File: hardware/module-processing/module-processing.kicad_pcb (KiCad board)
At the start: 2 copper layers, 64 x 93.5 mm, 64 parts, among them IC1 PIC24FJ256GA702-I_SO, J1 Conn_02x10_Odd_Even, J2 Raspberry_Pi_2_3, J3 ICSP, Q1 Q_NPN_EBC, Q2 Q_NPN_EBC, Q3 Q_NPN_EBC, Q4 Q_NPN_EBC, U1 74HC595, Y1 MCSJK-7U-32.00-12-30-60-B-30

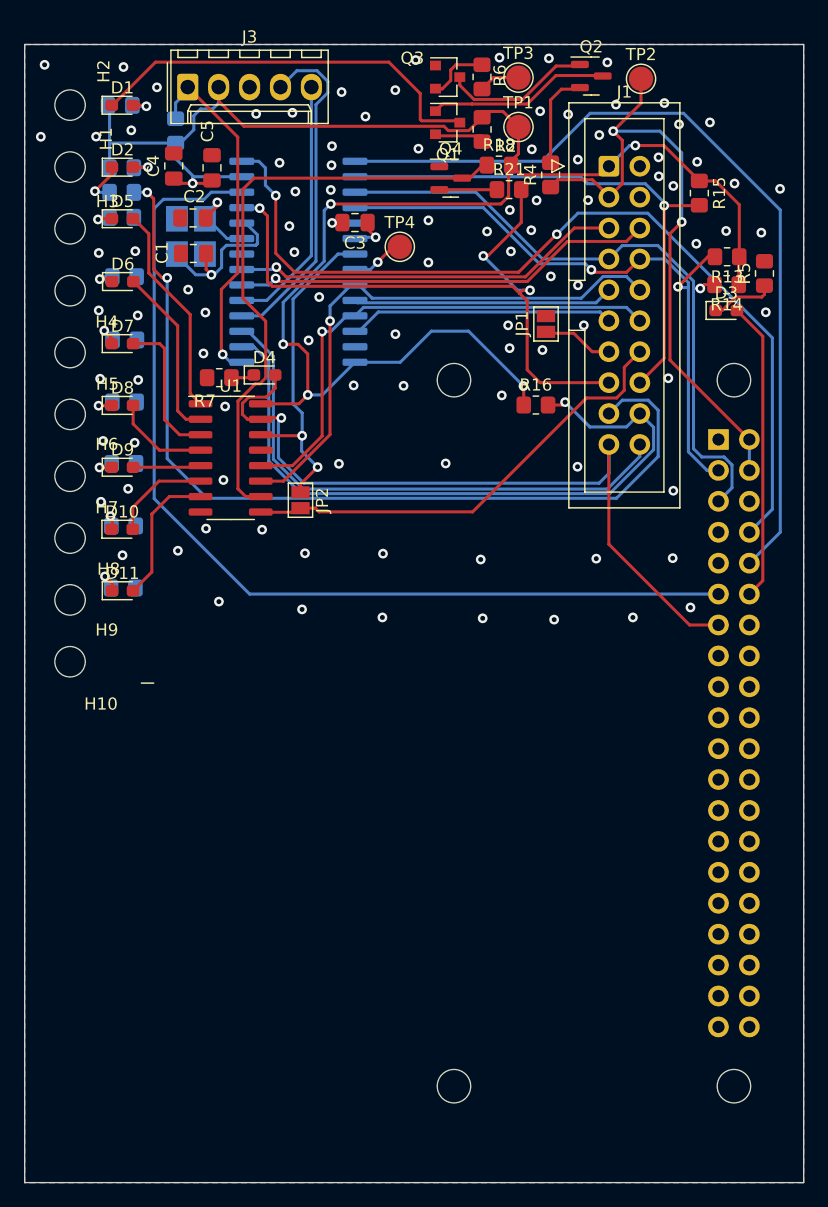
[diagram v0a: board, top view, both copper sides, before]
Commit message: fix: move pi to sensible position; chore: tidy and check
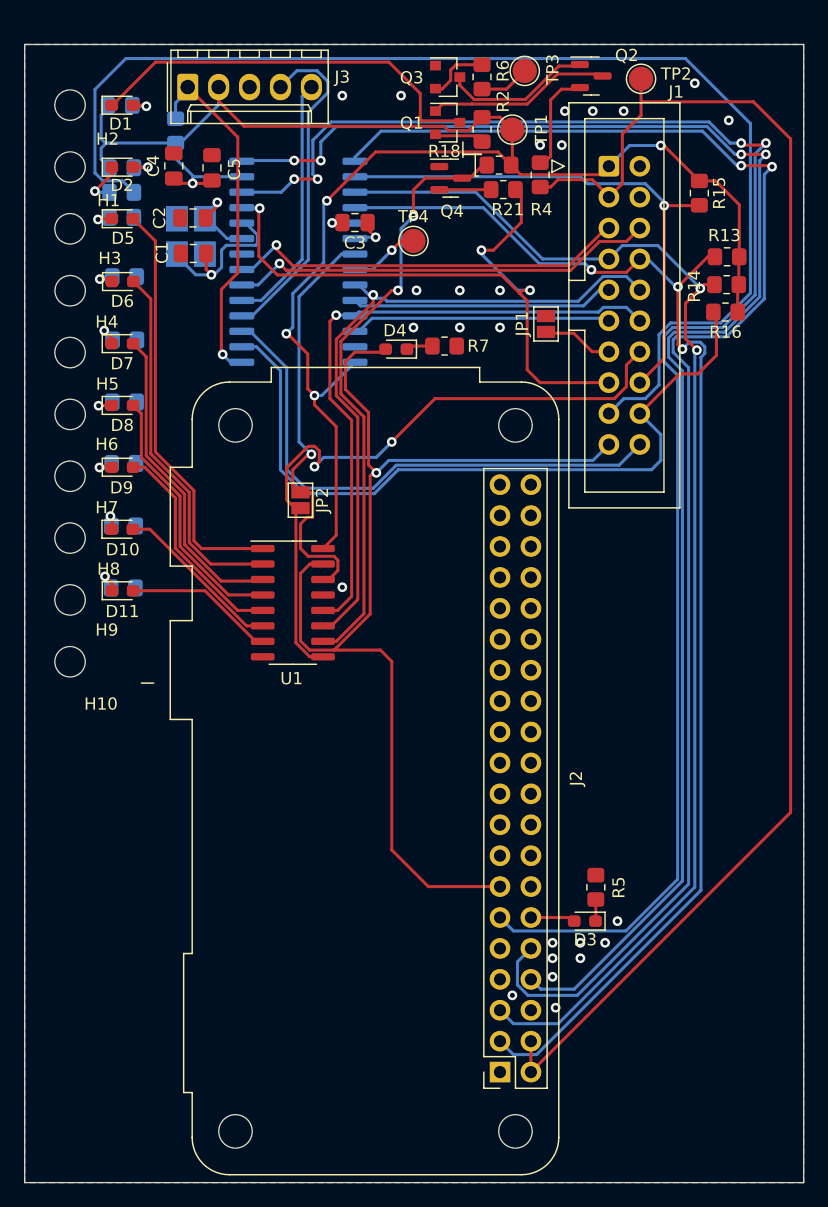
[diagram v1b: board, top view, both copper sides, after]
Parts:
- J2: moved to F.Cu
- moved J2 55.0 mm to (162.1, 108.9)
- moved R5 52.3 mm to (169.9, 93.7)
- moved D3 51.5 mm to (169.0, 96.5), turned to 180 degrees
- moved R7 18.7 mm to (157.5, 49.3), turned to 0 degrees
- moved R16 17.3 mm to (180.6, 46.5), turned to 180 degrees
- moved U1 12.9 mm to (145.0, 70.4)
- moved D4 11.0 mm to (153.5, 49.5), turned to 180 degrees
- moved TP4 1.22 mm to (154.9, 40.6)
- moved R4 0.86 mm to (165.4, 35.2)
- moved TP3 0.75 mm to (164.1, 26.7)
- moved TP1 0.55 mm to (163.1, 31.5)
- moved R21 0.48 mm to (162.3, 36.4)
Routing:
- net +5V: track 52.6 -> 118.8 mm, vias 2 -> 0
- net /Backplane/SDA: track 52.8 -> 108.4 mm, vias 2 -> 3
- net /Pi/PI_TX: track 74.0 -> 128.1 mm, vias 2 -> 4
- net /Pi/PI_RX: track 69.9 -> 123.6 mm, vias 0 -> 2
- net /Pi/PI_IO: track 81.2 -> 132.5 mm, vias 0 -> 4
- net /Backplane/SCL: track 54.6 -> 105.1 mm, vias 1 -> 2
- net /Backplane/HBEAT: track 62.5 -> 91.2 mm
- net /Backplane/ID_RET: track 75.6 -> 99.9 mm, vias 2 -> 0
- net /Pi/PI_HBEAT: track 24.6 -> 3.26 mm
- net Net-(D5-Pad2): track 17.5 -> 34.4 mm
- net /Backplane/OUT_DO: track 37.5 -> 53.7 mm, vias 0 -> 2
- net Net-(D6-Pad2): track 14.3 -> 30.1 mm
- net Net-(D7-Pad2): track 12.1 -> 25.8 mm
- net Net-(D8-Pad2): track 7.95 -> 21.6 mm
- net Net-(D9-Pad2): track 5.32 -> 17.9 mm
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
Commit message: feat: add labels to io pcb; feat: add labels to cpu pcb
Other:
- board text added: "PLC Processor Module V1.0 02/22 AGSB (C) Trace Technical Services"
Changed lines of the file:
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@@
     (fp_line (start -1 -0.625) (end 1 -0.625) (layer "F.Fab") (width 0.1))
     (fp_line (start 1 0.625) (end -1 0.625) (layer "F.Fab") (width 0.1))
-    (pad "1" smd roundrect (at -1 0 90) (size 1.2 1.4) (layers "F.Cu" "F.Paste" "F.Mask") (roundrect_rratio 0.208333)
+    (pad "1" smd roundrect (at -1 0 90) (size 1.2 1.4) (layers "F.Cu" "F.Paste" "F.Mask") (roundrect_rratio 0.2083333333)
       (net 7 "Net-(D3-Pad1)") (pintype "passive"))
-    (pad "2" smd roundrect (at 1 0 90) (size 1.2 1.4) (layers "F.Cu" "F.Paste" "F.Mask") (roundrect_rratio 0.208333)
+    (pad "2" smd roundrect (at 1 0 90) (size 1.2 1.4) (layers "F.Cu" "F.Paste" "F.Mask") (roundrect_rratio 0.2083333333)
       (net 1 "0") (pintype "passive"))
     (model "${KICAD6_3DMODEL_DIR}/Resistor_SMD.3dshapes/R_0805_2012Metric.wrl"
@@
     (fp_line (start 1 -0.625) (end 1 0.625) (layer "F.Fab") (width 0.1))
     (fp_line (start -1 -0.625) (end 1 -0.625) (layer "F.Fab") (width 0.1))
-    (pad "1" smd roundrect (at -1 0) (size 1.2 1.4) (layers "F.Cu" "F.Paste" "F.Mask") (roundrect_rratio 0.208333)
+    (pad "1" smd roundrect (at -1 0) (size 1.2 1.4) (layers "F.Cu" "F.Paste" "F.Mask") (roundrect_rratio 0.2083333333)
       (net 80 "Net-(Q4-Pad2)") (pintype "passive"))
-    (pad "2" smd roundrect (at 1 0) (size 1.2 1.4) (layers "F.Cu" "F.Paste" "F.Mask") (roundrect_rratio 0.208333)
+    (pad "2" smd roundrect (at 1 0) (size 1.2 1.4) (layers "F.Cu" "F.Paste" "F.Mask") (roundrect_rratio 0.2083333333)
       (net 22 "/Backplane/RESET") (pintype "passive"))
     (model "${KICAD6_3DMODEL_DIR}/Resistor_SMD.3dshapes/R_0805_2012Metric.wrl"
@@
     (fp_line (start -1 -0.625) (end 1 -0.625) (layer "F.Fab") (width 0.1))
     (fp_line (start 1 -0.625) (end 1 0.625) (layer "F.Fab") (width 0.1))
-    (pad "1" smd roundrect (at -1 0 180) (size 1.2 1.4) (layers "F.Cu" "F.Paste" "F.Mask") (roundrect_rratio 0.208333)
+    (pad "1" smd roundrect (at -1 0 180) (size 1.2 1.4) (layers "F.Cu" "F.Paste" "F.Mask") (roundrect_rratio 0.2083333333)
       (net 2 "+3V3") (pintype "passive"))
-    (pad "2" smd roundrect (at 1 0 180) (size 1.2 1.4) (layers "F.Cu" "F.Paste" "F.Mask") (roundrect_rratio 0.208333)
+    (pad "2" smd roundrect (at 1 0 180) (size 1.2 1.4) (layers "F.Cu" "F.Paste" "F.Mask") (roundrect_rratio 0.2083333333)
       (net 23 "/Backplane/DA_IRET") (pintype "passive"))
     (model "${KICAD6_3DMODEL_DIR}/Resistor_SMD.3dshapes/R_0805_2012Metric.wrl"
@@
     (fp_line (start 1 -0.625) (end 1 0.625) (layer "F.Fab") (width 0.1))
     (fp_line (start 1 0.625) (end -1 0.625) (layer "F.Fab") (width 0.1))
-    (pad "1" smd roundrect (at -1 0 180) (size 1.2 1.4) (layers "F.Cu" "F.Paste" "F.Mask") (roundrect_rratio 0.208333)
+    (pad "1" smd roundrect (at -1 0 180) (size 1.2 1.4) (layers "F.Cu" "F.Paste" "F.Mask") (roundrect_rratio 0.2083333333)
       (net 2 "+3V3") (pintype "passive"))
-    (pad "2" smd roundrect (at 1 0 180) (size 1.2 1.4) (layers "F.Cu" "F.Paste" "F.Mask") (roundrect_rratio 0.208333)
+    (pad "2" smd roundrect (at 1 0 180) (size 1.2 1.4) (layers "F.Cu" "F.Paste" "F.Mask") (roundrect_rratio 0.2083333333)
       (net 16 "/Backplane/SDA") (pintype "passive"))
     (model "${KICAD6_3DMODEL_DIR}/Resistor_SMD.3dshapes/R_0805_2012Metric.wrl"
@@
     (fp_line (start 1 -0.625) (end 1 0.625) (layer "F.Fab") (width 0.1))
     (fp_line (start -1 0.625) (end -1 -0.625) (layer "F.Fab") (width 0.1))
-    (pad "1" smd roundrect (at -1.0375 0 180) (size 1.175 1.45) (layers "F.Cu" "F.Paste" "F.Mask") (roundrect_rratio 0.212766)
+    (pad "1" smd roundrect (at -1.0375 0 180) (size 1.175 1.45) (layers "F.Cu" "F.Paste" "F.Mask") (roundrect_rratio 0.2127659574)
       (net 38 "Net-(C3-Pad1)") (pintype "passive"))
-    (pad "2" smd roundrect (at 1.0375 0 180) (size 1.175 1.45) (layers "F.Cu" "F.Paste" "F.Mask") (roundrect_rratio 0.212766)
+    (pad "2" smd roundrect (at 1.0375 0 180) (size 1.175 1.45) (layers "F.Cu" "F.Paste" "F.Mask") (roundrect_rratio 0.2127659574)
       (net 1 "0") (pintype "passive"))
     (model "${KICAD6_3DMODEL_DIR}/Capacitor_SMD.3dshapes/C_0805_2012Metric.wrl"
@@
     (fp_line (start -1 0.625) (end -1 -0.625) (layer "F.Fab") (width 0.1))
     (fp_line (start 1 -0.625) (end 1 0.625) (layer "F.Fab") (width 0.1))
-    (pad "1" smd roundrect (at -1 0 180) (size 1.2 1.4) (layers "F.Cu" "F.Paste" "F.Mask") (roundrect_rratio 0.208333)
+    (pad "1" smd roundrect (at -1 0 180) (size 1.2 1.4) (layers "F.Cu" "F.Paste" "F.Mask") (roundrect_rratio 0.2083333333)
       (net 2 "+3V3") (pintype "passive"))
-    (pad "2" smd roundrect (at 1 0 180) (size 1.2 1.4) (layers "F.Cu" "F.Paste" "F.Mask") (roundrect_rratio 0.208333)
+    (pad "2" smd roundrect (at 1 0 180) (size 1.2 1.4) (layers "F.Cu" "F.Paste" "F.Mask") (roundrect_rratio 0.2083333333)
       (net 17 "/Backplane/SCL") (pintype "passive"))
     (model "${KICAD6_3DMODEL_DIR}/Resistor_SMD.3dshapes/R_0805_2012Metric.wrl"
@@
     (fp_line (start 1 -0.625) (end 1 0.625) (layer "F.Fab") (width 0.1))
     (fp_line (start -1 -0.625) (end 1 -0.625) (layer "F.Fab") (width 0.1))
-    (pad "1" smd roundrect (at -1 0 270) (size 1.2 1.4) (layers "F.Cu" "F.Paste" "F.Mask") (roundrect_rratio 0.208333)
+    (pad "1" smd roundrect (at -1 0 270) (size 1.2 1.4) (layers "F.Cu" "F.Paste" "F.Mask") (roundrect_rratio 0.2083333333)
       (net 2 "+3V3") (pintype "passive"))
-    (pad "2" smd roundrect (at 1 0 270) (size 1.2 1.4) (layers "F.Cu" "F.Paste" "F.Mask") (roundrect_rratio 0.208333)
+    (pad "2" smd roundrect (at 1 0 270) (size 1.2 1.4) (layers "F.Cu" "F.Paste" "F.Mask") (roundrect_rratio 0.2083333333)
       (net 18 "/Backplane/IRQ") (pintype "passive"))
     (model "${KICAD6_3DMODEL_DIR}/Resistor_SMD.3dshapes/R_0805_2012Metric.wrl"
@@
     (fp_line (start 1 -0.625) (end 1 0.625) (layer "F.Fab") (width 0.1))
     (fp_line (start -1 -0.625) (end 1 -0.625) (layer "F.Fab") (width 0.1))
-    (pad "1" smd roundrect (at -1 0 90) (size 1.2 1.4) (layers "F.Cu" "F.Paste" "F.Mask") (roundrect_rratio 0.208333)
+    (pad "1" smd roundrect (at -1 0 90) (size 1.2 1.4) (layers "F.Cu" "F.Paste" "F.Mask") (roundrect_rratio 0.2083333333)
       (net 26 "+5V") (pintype "passive"))
-    (pad "2" smd roundrect (at 1 0 90) (size 1.2 1.4) (layers "F.Cu" "F.Paste" "F.Mask") (roundrect_rratio 0.208333)
+    (pad "2" smd roundrect (at 1 0 90) (size 1.2 1.4) (layers "F.Cu" "F.Paste" "F.Mask") (roundrect_rratio 0.2083333333)
       (net 31 "Net-(Q2-Pad2)") (pintype "passive"))
     (model "${KICAD6_3DMODEL_DIR}/Resistor_SMD.3dshapes/R_0805_2012Metric.wrl"
@@
     (fp_line (start -1 -0.625) (end 1 -0.625) (layer "F.Fab") (width 0.1))
     (fp_line (start 1 -0.625) (end 1 0.625) (layer "F.Fab") (width 0.1))
-    (pad "1" smd roundrect (at -1 0) (size 1.2 1.4) (layers "F.Cu" "F.Paste" "F.Mask") (roundrect_rratio 0.208333)
+    (pad "1" smd roundrect (at -1 0) (size 1.2 1.4) (layers "F.Cu" "F.Paste" "F.Mask") (roundrect_rratio 0.2083333333)
       (net 81 "Net-(Q4-Pad3)") (pintype "passive"))
-    (pad "2" smd roundrect (at 1 0) (size 1.2 1.4) (layers "F.Cu" "F.Paste" "F.Mask") (roundrect_rratio 0.208333)
+    (pad "2" smd roundrect (at 1 0) (size 1.2 1.4) (layers "F.Cu" "F.Paste" "F.Mask") (roundrect_rratio 0.2083333333)
       (net 2 "+3V3") (pintype "passive"))
     (model "${KICAD6_3DMODEL_DIR}/Resistor_SMD.3dshapes/R_0805_2012Metric.wrl"
@@
   (gr_line (start 187 118) (end 123 118) (layer "Edge.Cuts") (width 0.05))
   (gr_line (start 187 24.5) (end 187 118) (layer "Edge.Cuts") (width 0.05))
+  (gr_text "PLC Processor Module\nV1.0 02/22 AGSB\n(C) Trace Technical Services" (at 178.308 92.964 90) (layer "F.SilkS")
+    (effects (font (size 1.5 1.5) (thickness 0.3)))
+  )
   (gr_text "CL" (at 126.73 27.08) (layer "Dwgs.User")
     (effects (font (size 1 1) (thickness 0.15)))
